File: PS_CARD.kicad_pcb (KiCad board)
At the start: 2 copper layers, 132.7 x 74.8 mm, 34 parts, among them J1 430450402, J2 430451602

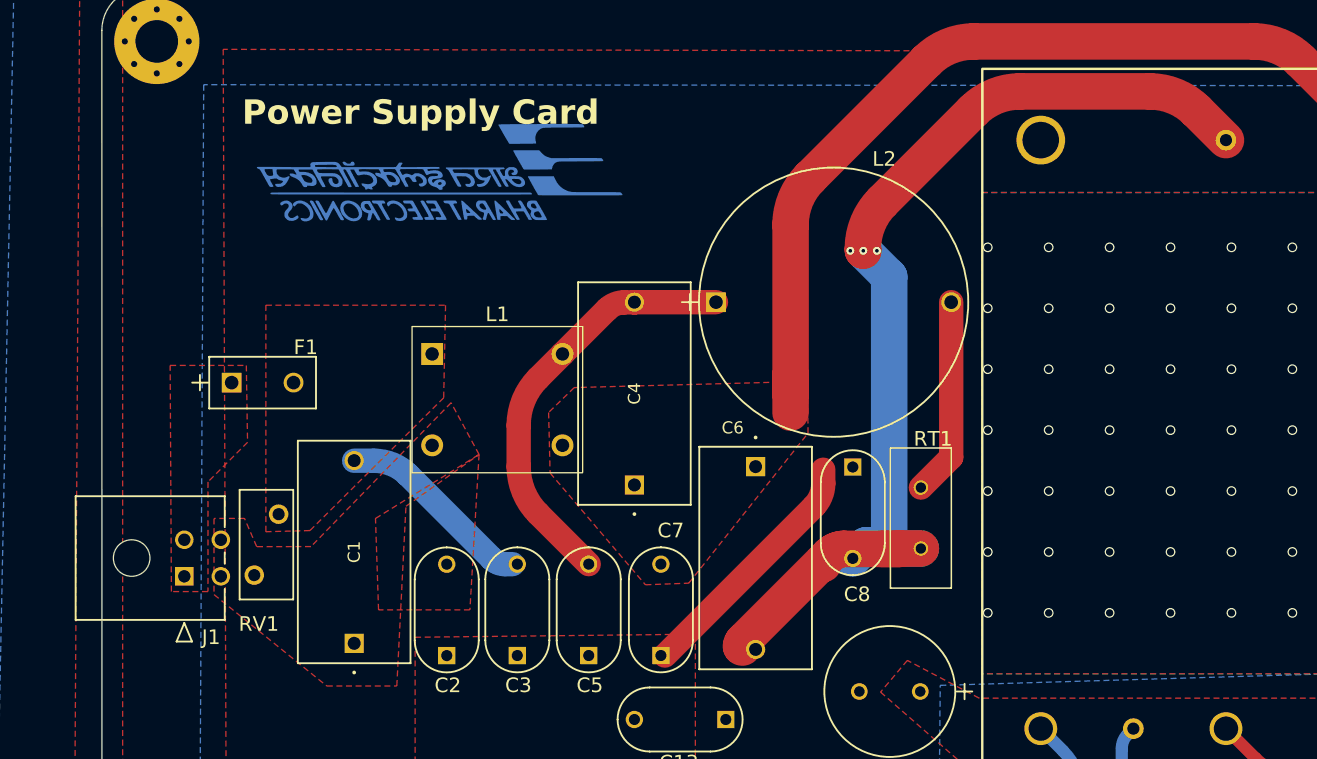
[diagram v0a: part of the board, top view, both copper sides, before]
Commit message: Shifted the connector
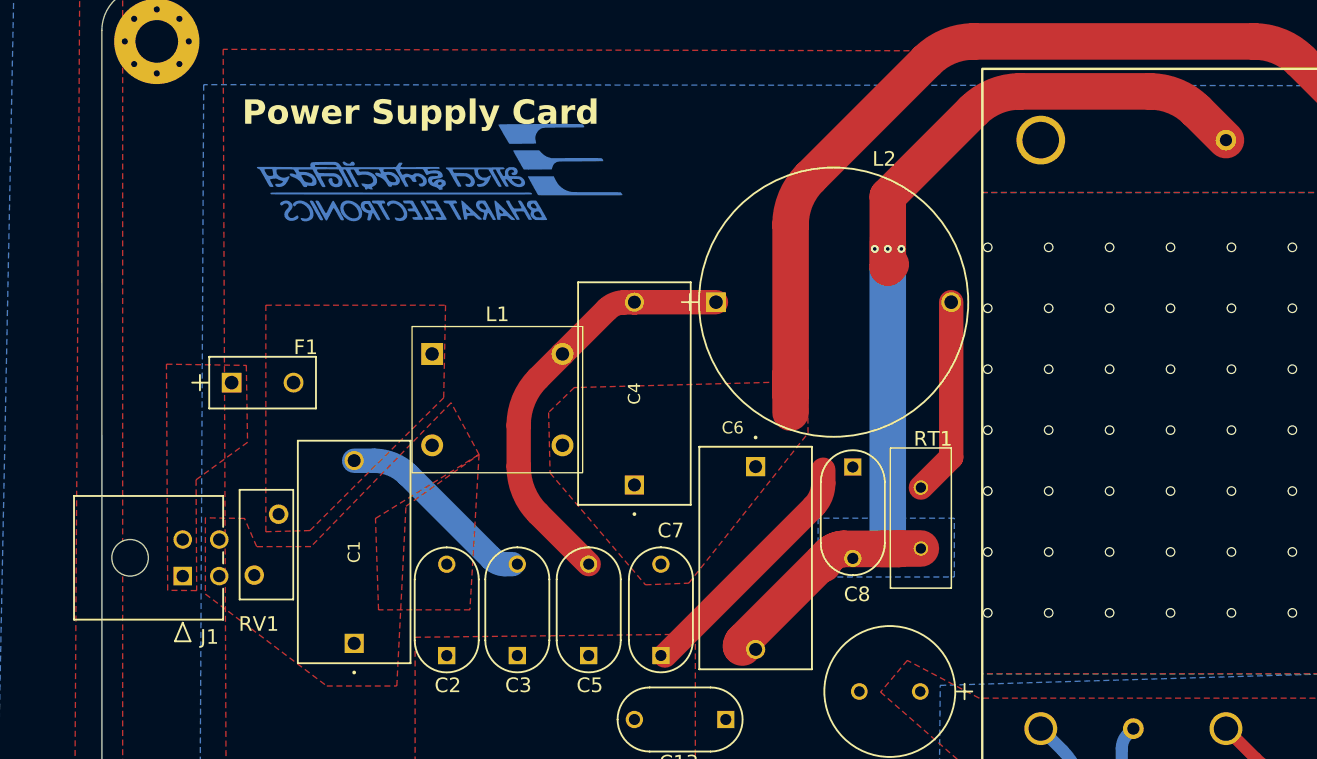
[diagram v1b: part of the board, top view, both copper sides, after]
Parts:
- moved J1 0.13 mm to (63.9, 114.5)
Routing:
- net Net-(U1-AC1): track 100.3 -> 94.7 mm
- added copper zone on B.Cu, net Net-(U1-AC1)
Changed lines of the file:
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@@
 			(pintype "passive")
 			(solder_mask_margin 0.102)
+			(zone_connect 2)
 			(teardrops
 				(best_length_ratio 0.5)
@@
 			(net 3 "Net-(U1-AC1)")
 			(pintype "unspecified")
+			(zone_connect 2)
 			(teardrops
 				(best_length_ratio 0.5)
@@
 	(footprint "mohit:430450402_MOL"
 		(layer "F.Cu")
-		(at 64.0588 114.5 -90)
+		(at 63.929001 114.4792 -90)
 		(tags "430450402 ")
 		(property "Reference" "J1"
@@
 	)
 	(segment
+		(start 121.793 83.306999)
+		(end 121.793 89.154)
+		(width 3)
+		(layer "F.Cu")
+		(net 3)
+	)
+	(segment
+		(start 149.55 78.7)
+		(end 147.143792 76.293792)
+		(width 3)
+		(layer "F.Cu")
+		(net 3)
+	)
+	(segment
 		(start 122.75 112.25)
 		(end 121.25 112.25)
@@
 	)
 	(segment
-		(start 119.75 87.603963)
-		(end 119.75 87.746)
+		(start 121.793 89.154)
+		(end 122.047 88.9)
 		(width 3)
 		(layer "F.Cu")
@@
 	)
 	(segment
-		(start 147.143792 76.293792)
-		(end 149.55 78.7)
-		(width 3)
-		(layer "F.Cu")
-		(net 3)
-	)
-	(segment
-		(start 119.75 87.746)
-		(end 119.7864 87.7824)
+		(start 128.806207 76.293792)
+		(end 121.793 83.306999)
 		(width 3)
 		(layer "F.Cu")
@@
 	)
 	(segment
-		(start 128.806207 76.293792)
-		(end 121.343792 83.756207)
-		(width 3)
-		(layer "F.Cu")
-		(net 3)
-	)
-	(segment
 		(start 122.7828 112.2172)
 		(end 124.5108 112.2172)
@@
 	)
 	(segment
-		(start 132.653963 74.7)
-		(end 143.296036 74.7)
+		(start 143.296036 74.7)
+		(end 132.653963 74.7)
 		(width 3)
 		(layer "F.Cu")
@@
 	)
 	(via
-		(at 119.7864 87.7824)
+		(at 121.793 87.63)
 		(size 0.65)
 		(drill 0.3)
@@
 	)
 	(via
-		(at 120.904 87.7824)
+		(at 122.9106 87.63)
 		(size 0.65)
 		(drill 0.3)
@@
 	)
 	(via
-		(at 118.7196 87.7824)
+		(at 120.7262 87.63)
 		(size 0.65)
 		(drill 0.3)
@@
 	)
 	(arc
-		(start 128.806207 76.293792)
+		(start 132.653963 74.7)
 		(mid 130.571572 75.114213)
-		(end 132.653963 74.7)
+		(end 128.806207 76.293792)
 		(width 3)
 		(layer "F.Cu")
@@
 	)
 	(arc
+		(start 147.143792 76.293792)
+		(mid 145.378426 75.114213)
+		(end 143.296036 74.7)
+		(width 3)
+		(layer "F.Cu")
+		(net 3)
+	)
+	(arc
 		(start 109.921826 120.314173)
 		(mid 109.812134 120.335992)
@@
 	)
 	(arc
-		(start 143.296036 74.7)
-		(mid 145.378426 75.114213)
-		(end 147.143792 76.293792)
-		(width 3)
-		(layer "F.Cu")
-		(net 3)
-	)
-	(arc
 		(start 109.921826 119.828173)
 		(mid 109.794656 120.018497)
@@
 	)
 	(arc
-		(start 121.343792 83.756207)
-		(mid 120.164213 85.521572)
-		(end 119.75 87.603963)
-		(width 3)
-		(layer "F.Cu")
-		(net 3)
-	)
-	(arc
 		(start 117 112.75)
 		(mid 117.553825 112.379945)
@@
 	)
 	(segment
-		(start 119.9988 111.954)
-		(end 118.9228 113.03)
-		(width 3)
-		(layer "B.Cu")
-		(net 3)
-	)
-	(segment
-		(start 119.7864 87.7824)
-		(end 121.9108 89.9068)
-		(width 3)
-		(layer "B.Cu")
-		(net 3)
-	)
-	(segment
-		(start 122.174 112.2172)
-		(end 121.9108 111.954)
-		(width 3)
-		(layer "B.Cu")
-		(net 3)
-	)
-	(segment
-		(start 121.9108 89.9068)
-		(end 121.9108 111.954)
-		(width 3)
-		(layer "B.Cu")
-		(net 3)
-	)
-	(segment
-		(start 124.5108 112.2172)
-		(end 122.174 112.2172)
-		(width 3)
-		(layer "B.Cu")
-		(net 3)
-	)
-	(segment
-		(start 121.9108 111.954)
-		(end 119.9988 111.954)
+		(start 121.793 86.995)
+		(end 121.793 111.379)
 		(width 3)
 		(layer "B.Cu")
@@
 		(polygon
 			(pts
-				(xy 66.5 109.75) (xy 66.5 116) (xy 75.75 123.5) (xy 81.5 123.5) (xy 82.25 108.75) (xy 88.25 104.5)
+				(xy 65.7888 109.6992) (xy 65.7888 115.9492) (xy 75.75 123.5) (xy 81.5 123.5) (xy 82.25 108.75) (xy 88.25 104.5)
 				(xy 85.9572 100.254) (xy 74.4572 112.0588) (xy 70.0024 112.0648) (xy 69 109.75)
 			)
@@
 		(polygon
 			(pts
-				(xy 63 115.75) (xy 62.8984 97.19) (xy 69.1484 97.19) (xy 69.25 103.5) (xy 66 106.75) (xy 66 115.75)
+				(xy 62.6952 115.6484) (xy 62.5936 97.0884) (xy 69.1484 97.19) (xy 69.25 103.5) (xy 65.024 106.5784)
+				(xy 65.0748 115.6716)
 			)
 		)
@@
 		(filled_areas_thickness no)
 		(keepout
-			(tracks not_allowed)
-			(vias not_allowed)
-			(pads not_allowed)
-			(copperpour not_allowed)
-			(footprints allowed)
-		)
-		(fill
-			(thermal_gap 0.5)
-			(thermal_bridge_width 0.5)
-			(island_removal_mode 1)
-			(island_area_min 10)
-		)
-		(polygon
-			(pts
-				(xy 66.25 109.75) (xy 66.25 114.5) (xy 65.8 114.5) (xy 65.8 109.75)
-			)
-		)
-	)
-	(zone
-		(net 0)
-		(net_name "")
-		(layer "F.Cu")
-		(hatch edge 0.5)
-		(connect_pads thru_hole_only
-			(clearance 0)
-		)
-		(min_thickness 0.25)
-		(filled_areas_thickness no)
-		(keepout
 			(tracks allowed)
 			(vias allowed)
@@
 	)
 	(zone
+		(net 3)
+		(net_name "Net-(U1-AC1)")
+		(layer "B.Cu")
+		(hatch edge 0.5)
+		(priority 12)
+		(connect_pads
+			(clearance 0.5)
+		)
+		(min_thickness 0.25)
+		(filled_areas_thickness no)
+		(fill yes
+			(thermal_gap 0.5)
+			(thermal_bridge_width 0.5)
+		)
+		(polygon
+			(pts
+				(xy 127.254 109.728) (xy 116.078 109.728) (xy 116.078 114.554) (xy 127.254 114.554)
+			)
+		)
+	)
+	(zone
 		(net 4)
 		(net_name "GNDPWR")
@@
 	)
 	(zone
-		(net 12)
-		(net_name "/Trim")
+		(net 7)
+		(net_name "+28V")
 		(layer "B.Cu")
 		(name "$teardrop_padvia$")
 		(hatch full 0.1)
-		(priority 30000)
+		(priority 30001)
 		(attr
 			(teardrop
@@
 		(polygon
 			(pts
-				(xy 140.522891 128.317371) (xy 141.514339 128.447871) (xy 142.551041 127.601041) (xy 141.95013 126.999009)
-				(xy 141.164702 126.674719)
+				(xy 148.27524 137.767695) (xy 148.97476 138.482305) (xy 150.044601 137.7112) (xy 149.750714 136.999301)
+				(xy 149.0388 136.705424)
 			)
 		)
@@
 	)
 	(zone
-		(net 7)
-		(net_name "+28V")
+		(net 0)
+		(net_name "")
 		(layer "B.Cu")
-		(name "$teardrop_padvia$")
-		(hatch full 0.1)
-		(priority 30001)
-		(attr
-			(teardrop
-				(type padvia)
-			)
-		)
-		(connect_pads yes
+		(hatch edge 0.5)
+		(connect_pads thru_hole_only
 			(clearance 0)
 		)
-		(min_thickness 0.0254)
+		(min_thickness 0.25)
 		(filled_areas_thickness no)
-		(fill yes
+		(keepout
+			(tracks allowed)
+			(vias allowed)
+			(pads allowed)
+			(copperpour not_allowed)
+			(footprints allowed)
+		)
+		(fill
 			(thermal_gap 0.5)
 			(thermal_bridge_width 0.5)
@@
 		(polygon
 			(pts
-				(xy 148.27524 137.767695) (xy 148.97476 138.482305) (xy 150.044601 137.7112) (xy 149.750714 136.999301)
-				(xy 149.0388 136.705424)
+				(xy 67 112.15) (xy 67.1 113.25) (xy 66.35 113.7) (xy 65.85 112.85) (xy 65.9 112.5) (xy 66.35 112.15)
 			)
 		)
 	)
 	(zone
-		(net 0)
-		(net_name "")
+		(net 12)
+		(net_name "/Trim")
 		(layer "B.Cu")
-		(hatch edge 0.5)
-		(connect_pads thru_hole_only
+		(name "$teardrop_padvia$")
+		(hatch full 0.1)
+		(priority 30000)
+		(attr
+			(teardrop
+				(type padvia)
+			)
+		)
+		(connect_pads yes
 			(clearance 0)
 		)
-		(min_thickness 0.25)
+		(min_thickness 0.0254)
 		(filled_areas_thickness no)
-		(keepout
-			(tracks allowed)
-			(vias allowed)
-			(pads allowed)
-			(copperpour not_allowed)
-			(footprints allowed)
-		)
-		(fill
+		(fill yes
 			(thermal_gap 0.5)
 			(thermal_bridge_width 0.5)
@@
 		(polygon
 			(pts
-				(xy 67 112.15) (xy 67.1 113.25) (xy 66.35 113.7) (xy 65.85 112.85) (xy 65.9 112.5) (xy 66.35 112.15)
+				(xy 140.522891 128.317371) (xy 141.514339 128.447871) (xy 142.551041 127.601041) (xy 141.95013 126.999009)
+				(xy 141.164702 126.674719)
 			)
 		)

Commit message: Added stiching vias, changed constraints as per MIL275
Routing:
- net GNDPWR: vias 42 -> 211

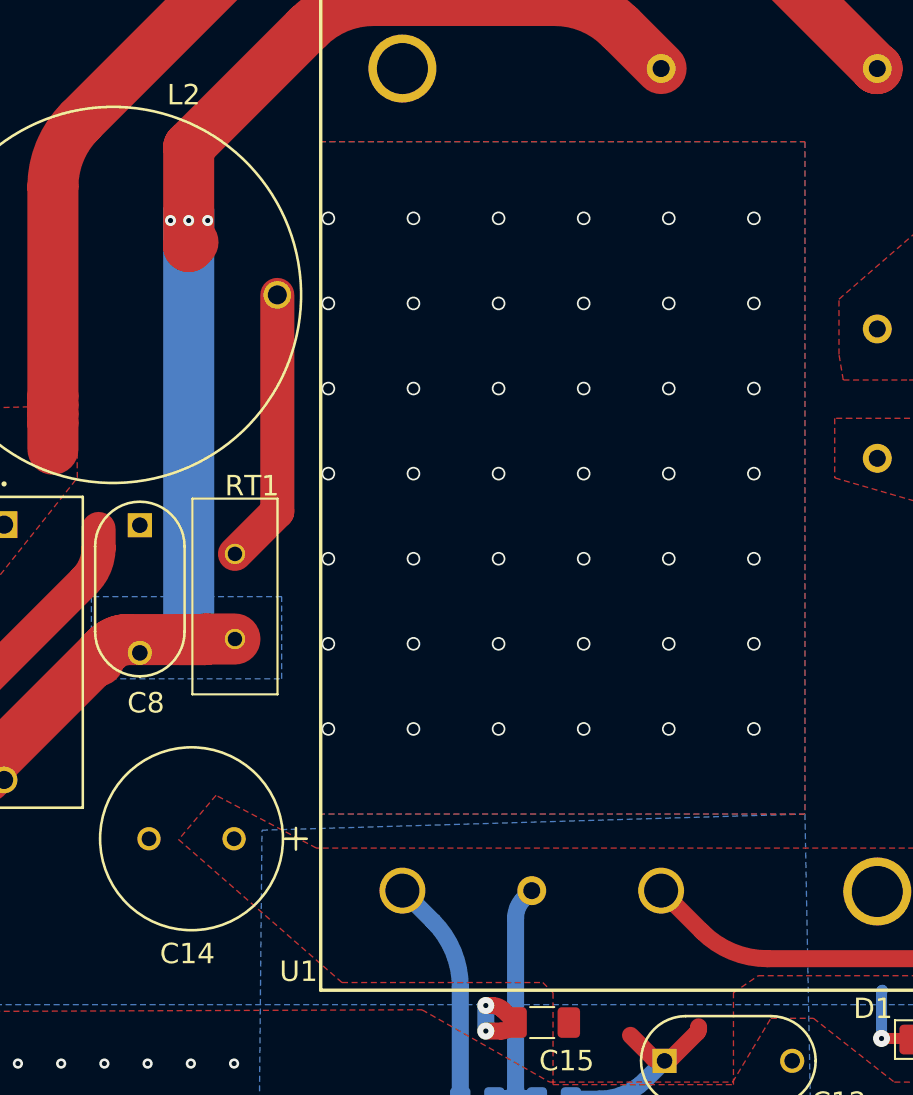
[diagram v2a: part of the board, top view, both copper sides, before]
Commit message: repositioned silk screen(MINOR)
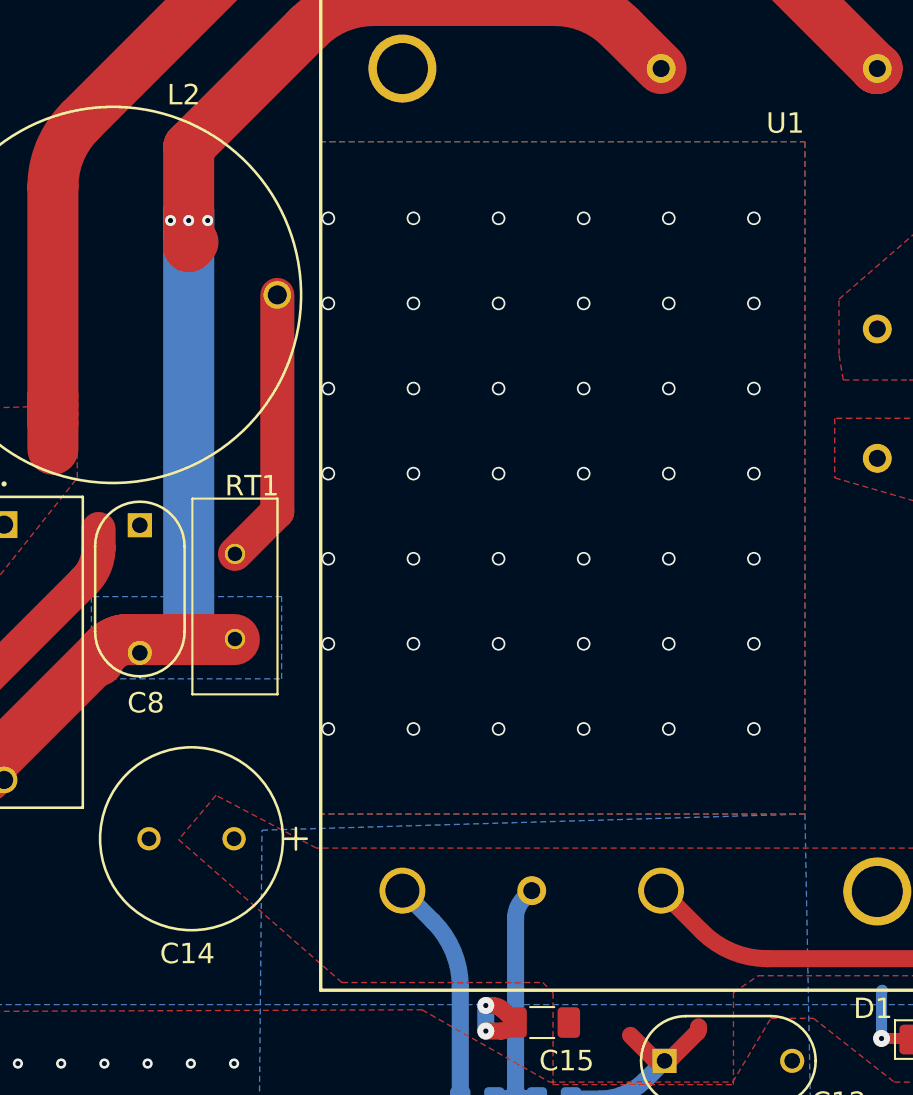
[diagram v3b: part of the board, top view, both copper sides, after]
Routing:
- net Net-(U1-AC1): track 94.7 -> 93.1 mm
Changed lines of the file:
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@@
 		(at 149.55 102.85 90)
 		(property "Reference" "U1"
-			(at -28.9 -21.3 0)
+			(at 20.935 7.295 0)
 			(unlocked yes)
 			(layer "F.SilkS" knockout)
@@
 	)
 	(segment
-		(start 149.55 78.7)
-		(end 147.143792 76.293792)
+		(start 124.478 112.25)
+		(end 118.207106 112.25)
 		(width 3)
 		(layer "F.Cu")
@@
 	)
 	(segment
-		(start 122.75 112.25)
-		(end 121.25 112.25)
+		(start 149.55 78.7)
+		(end 147.143792 76.293792)
 		(width 3)
 		(layer "F.Cu")
@@
 	)
 	(segment
-		(start 122.75 112.25)
-		(end 122.7828 112.2172)
-		(width 3)
-		(layer "F.Cu")
-		(net 3)
-	)
-	(segment
-		(start 122.75 112.25)
-		(end 118.207106 112.25)
-		(width 3)
-		(layer "F.Cu")
-		(net 3)
-	)
-	(segment
-		(start 122.7828 112.2172)
-		(end 124.5108 112.2172)
-		(width 3)
-		(layer "F.Cu")
-		(net 3)
-	)
-	(segment
 		(start 143.296036 74.7)
 		(end 132.653963 74.7)
@@
 	)
 	(zone
-		(net 12)
-		(net_name "/Trim")
-		(layer "B.Cu")
-		(name "$teardrop_padvia$")
-		(hatch full 0.1)
-		(priority 30000)
-		(attr
-			(teardrop
-				(type padvia)
-			)
-		)
-		(connect_pads yes
-			(clearance 0)
-		)
-		(min_thickness 0.0254)
-		(filled_areas_thickness no)
-		(fill yes
-			(thermal_gap 0.5)
-			(thermal_bridge_width 0.5)
-			(island_removal_mode 1)
-			(island_area_min 10)
-		)
-		(polygon
-			(pts
-				(xy 140.522891 128.317371) (xy 141.514339 128.447871) (xy 142.551041 127.601041) (xy 141.95013 126.999009)
-				(xy 141.164702 126.674719)
-			)
-		)
-	)
-	(zone
 		(net 0)
 		(net_name "")
@@
 			)
 		)
+	)
+	(zone
+		(net 12)
+		(net_name "/Trim")
+		(layer "B.Cu")
+		(name "$teardrop_padvia$")
+		(hatch full 0.1)
+		(priority 30000)
+		(attr
+			(teardrop
+				(type padvia)
+			)
+		)
+		(connect_pads yes
+			(clearance 0)
+		)
+		(min_thickness 0.0254)
+		(filled_areas_thickness no)
+		(fill yes
+			(thermal_gap 0.5)
+			(thermal_bridge_width 0.5)
+			(island_removal_mode 1)
+			(island_area_min 10)
+		)
+		(polygon
+			(pts
+				(xy 140.522891 128.317371) (xy 141.514339 128.447871) (xy 142.551041 127.601041) (xy 141.95013 126.999009)
+				(xy 141.164702 126.674719)
+			)
+		)
